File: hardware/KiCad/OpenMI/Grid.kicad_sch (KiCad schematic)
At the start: 42 parts, among them K1 G6DN-1ADC12, Q6 BSS123L, U5 MCP6004-SL, U6 CAP005DG

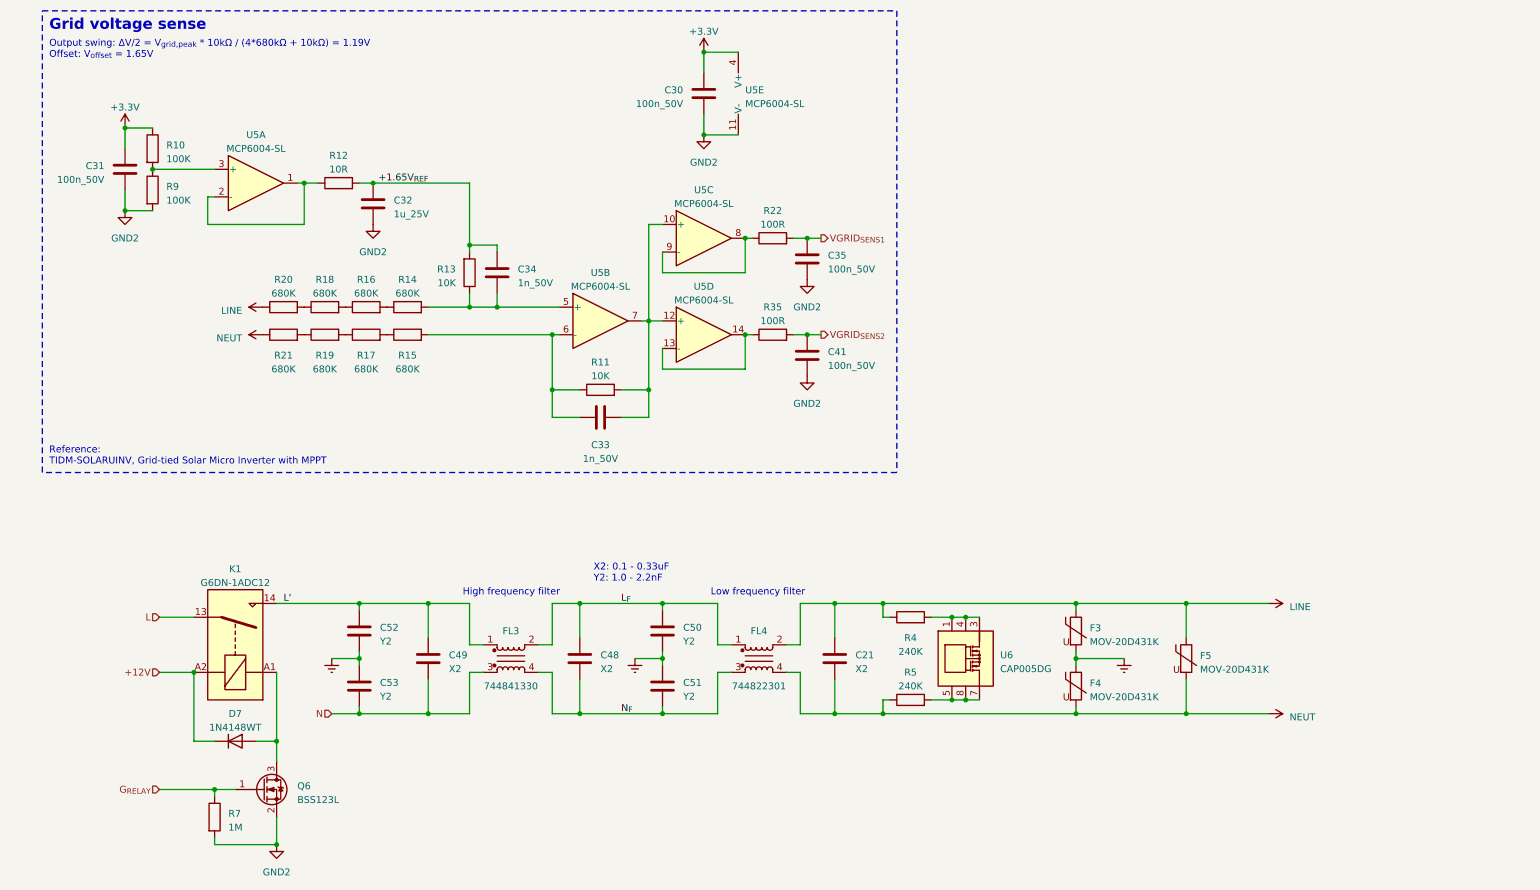
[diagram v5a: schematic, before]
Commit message: refactor(hw): Moves grid voltage sensing to `Sensing`. Refactors labels.
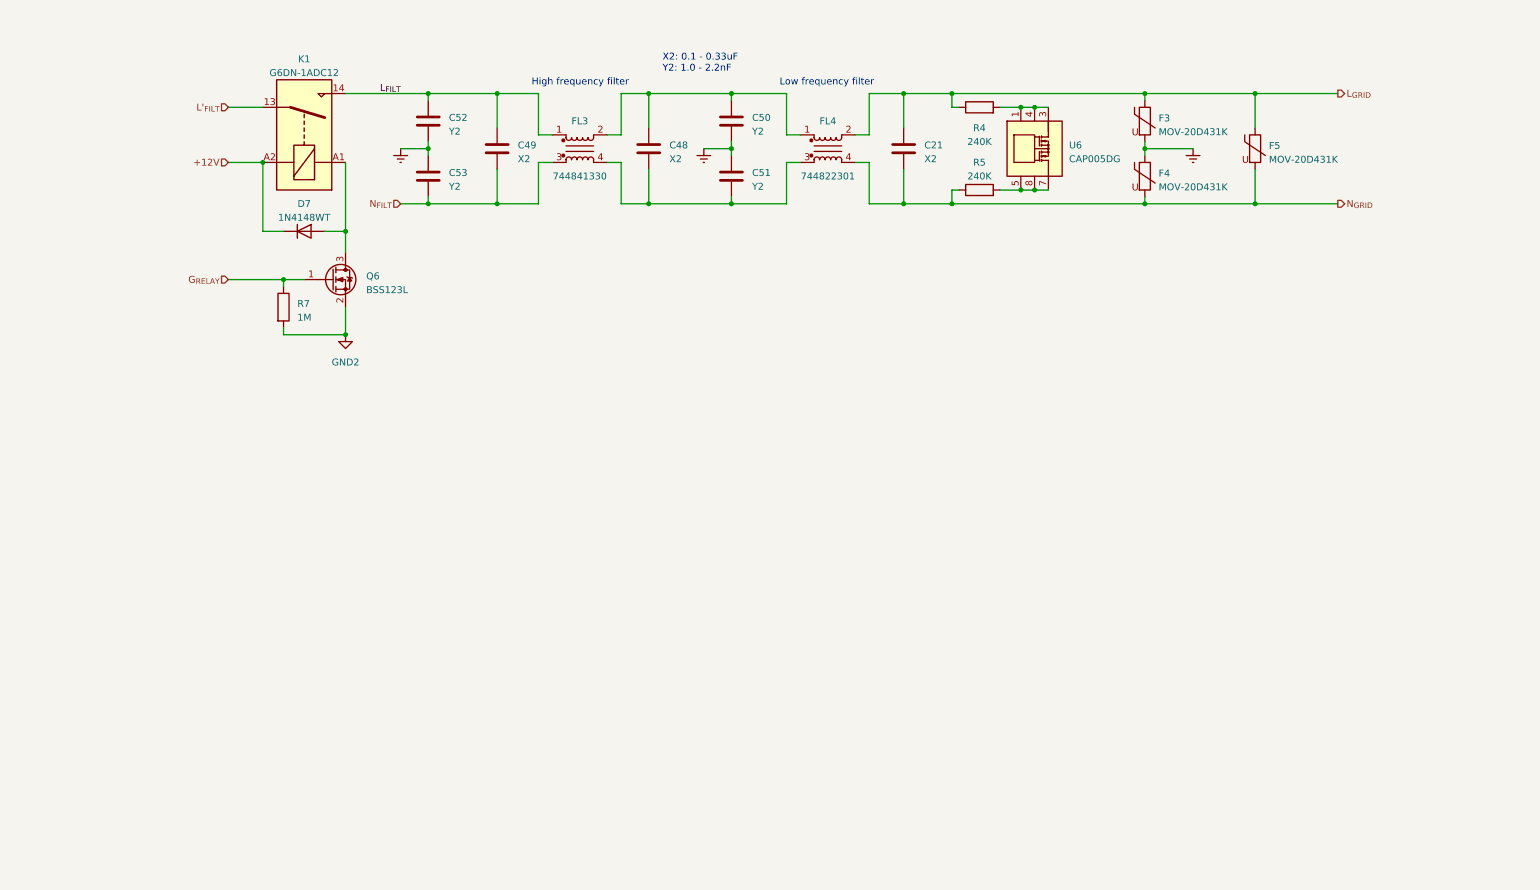
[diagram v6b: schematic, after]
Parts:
- removed C30, C31, C35, C41: 100n_50V, Capacitor_SMD:C_0603_1608Metric, symbol _C_0603:100n_50V
- removed C32: 1u_25V, Capacitor_SMD:C_0805_2012Metric, symbol _C_0805:1u_25V
- removed C33, C34: 1n_50V, Capacitor_SMD:C_0603_1608Metric, symbol _C_0603:1n_50V
- removed R10, R9: 100K, Resistor_SMD:R_0603_1608Metric, symbol _R_0603:100K
- removed R11, R13: 10K, Resistor_SMD:R_0603_1608Metric, symbol _R_0603:10K
- removed R12: 10R, Resistor_SMD:R_0603_1608Metric, symbol _R_0603:10R
- removed R14, R15, R16, R17, R18, R19, R20, R21: 680K, Resistor_SMD:R_1206_3216Metric, symbol _R_1206:680K
- removed R22, R35: 100R, Resistor_SMD:R_0603_1608Metric, symbol _R_0603:100R
- removed U5: MCP6004-SL, Package_SO:SOIC-14_3.9x8.7mm_P1.27mm, symbol _Amplifier_Operational:MCP6004-SL
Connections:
- net L renamed L'_{FILT}
- net L' renamed L_{FILT}
- net LINE renamed L_{GRID}
- net L_{F}: no longer names the net of C48.1, C50.1, FL3.2, FL4.1
- net N renamed N_{FILT}
- net NEUT renamed N_{GRID}
- net N_{F}: no longer names the net of C48.2, C51.2, FL3.4, FL4.3
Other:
- note removed: "Grid voltage sense"
- note removed: "Output swing: ΔV/2 = V_{grid,peak} * 10kΩ / (4*680kΩ + 10kΩ) = 1.19V Offset: V_{offset} = 1.65V"
- note removed: "Reference: TIDM-SOLARUINV, Grid-tied Solar Micro Inverter with MPPT"
- moved on the sheet: C21, C48, C49, C50, C51, C52, C53, D7, F3, F4, F5, FL3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

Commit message: refactor(hw): Adds final safety capacitors to line filter
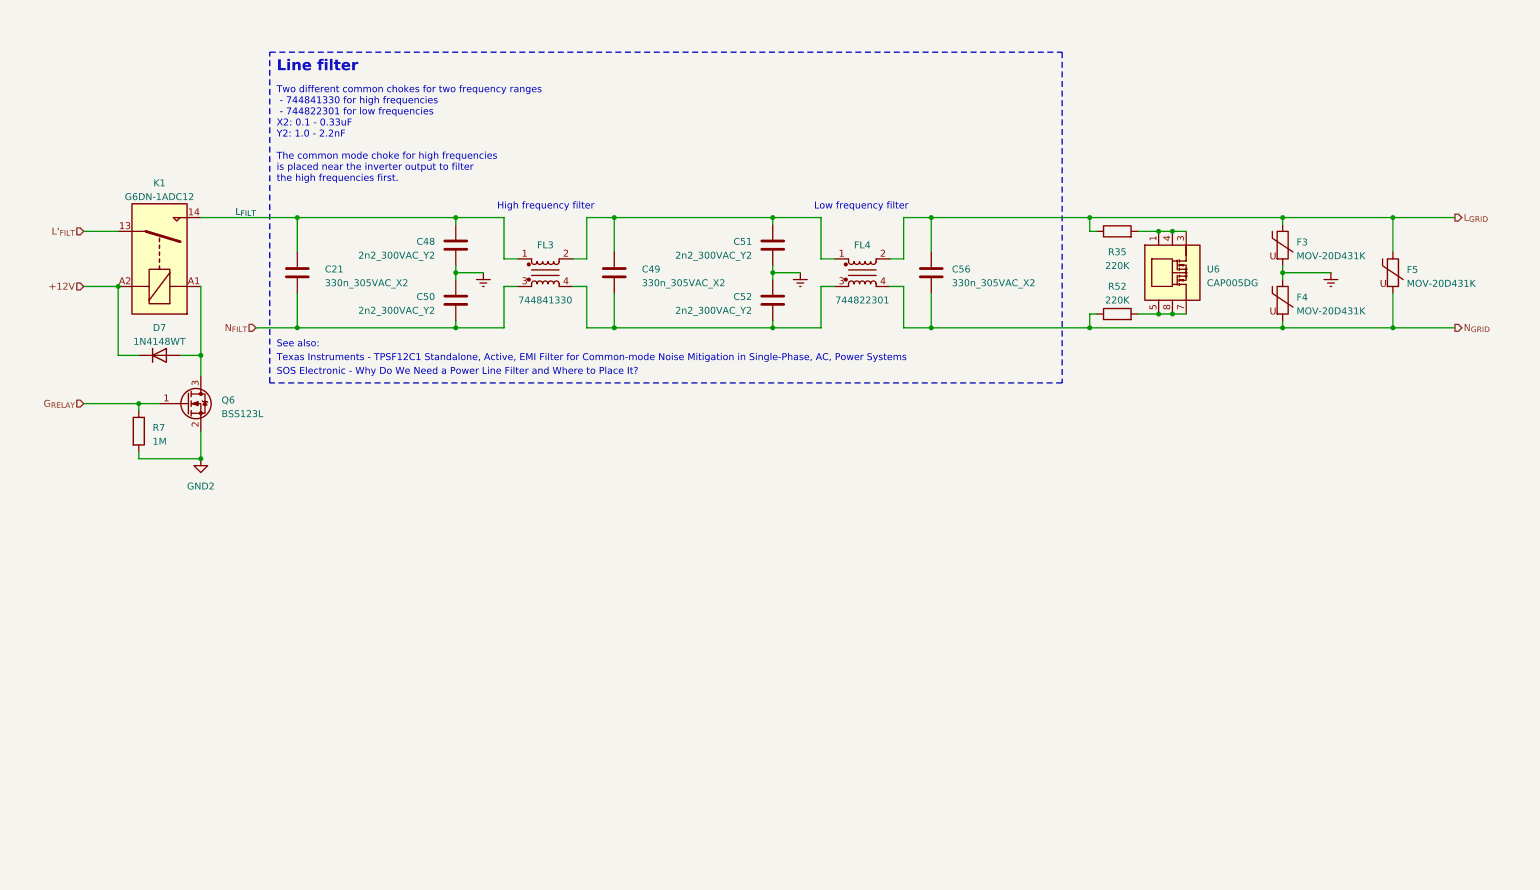
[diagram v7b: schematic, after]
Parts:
- removed C21, C48, C49: X2, symbol Device:C
- removed C50, C51, C52, C53: Y2, symbol Device:C
- removed R4, R5: 240K, Resistor_SMD:R_1206_3216Metric, symbol _R_1206:240K
- added C21, C49, C56: 330n_305VAC_X2, Capacitor_THT:C_Rect_L18.0mm_W8.0mm_P15.00mm_FKS3_FKP3, symbol _C_Safety:330n_305VAC_X2
- added C48, C50, C51, C52: 2n2_300VAC_Y2, Capacitor_THT:C_Rect_L13.0mm_W4.0mm_P10.00mm_FKS3_FKP3_MKS4, symbol _C_Safety:2n2_300VAC_Y2
- added R35, R52: 220K, Resistor_SMD:R_1206_3216Metric, symbol _R_1206:220K
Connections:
- net Earth: now also C48.2, C50.1, C51.2, C52.1
- net L_{FILT}: now also C21.1, C48.1
- net L_{GRID}: now also C56.1, R35.1
- net N_{FILT}: now also C21.2, C50.2
- net N_{GRID}: now also C56.2, R52.1
- net at FL3.2, FL4.1: now also C49.1, C51.1
- net at FL3.4, FL4.3: now also C49.2, C52.2
- net at U6.1, U6.2, U6.3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: now also R35.2
- net at U6.5, U6.6, U6.7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: now also R52.2
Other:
- note added: "Line filter"
- note added: "SOS Electronic - Why Do We Need a Power Line Filter and Where to Place It?"
- note added: "See also:"
- note added: "Texas Instruments - TPSF12C1 Standalone, Active, EMI Filter for Common-mode Noise Mitigation in Single-Phase, AC, Power Systems"
- note added: "Two different common chokes for two frequency ranges - 744841330 for high frequencies - 744822301 for low frequencies X2: 0.1 - 0.33uF Y2: 1.0 - 2.2nF The common mode choke for high frequencies is placed near the inverter output to filter the high frequencies first."
- note removed: "X2: 0.1 - 0.33uF Y2: 1.0 - 2.2nF"
- moved on the sheet: D7, F3, F4, F5, FL3, FL4, K1, Q6, R7, U6

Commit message: feat: Replaces SPST relay with DPDT relay to disconnect "neutral" as well.
docs: Add references to international standards for grid connected devices.
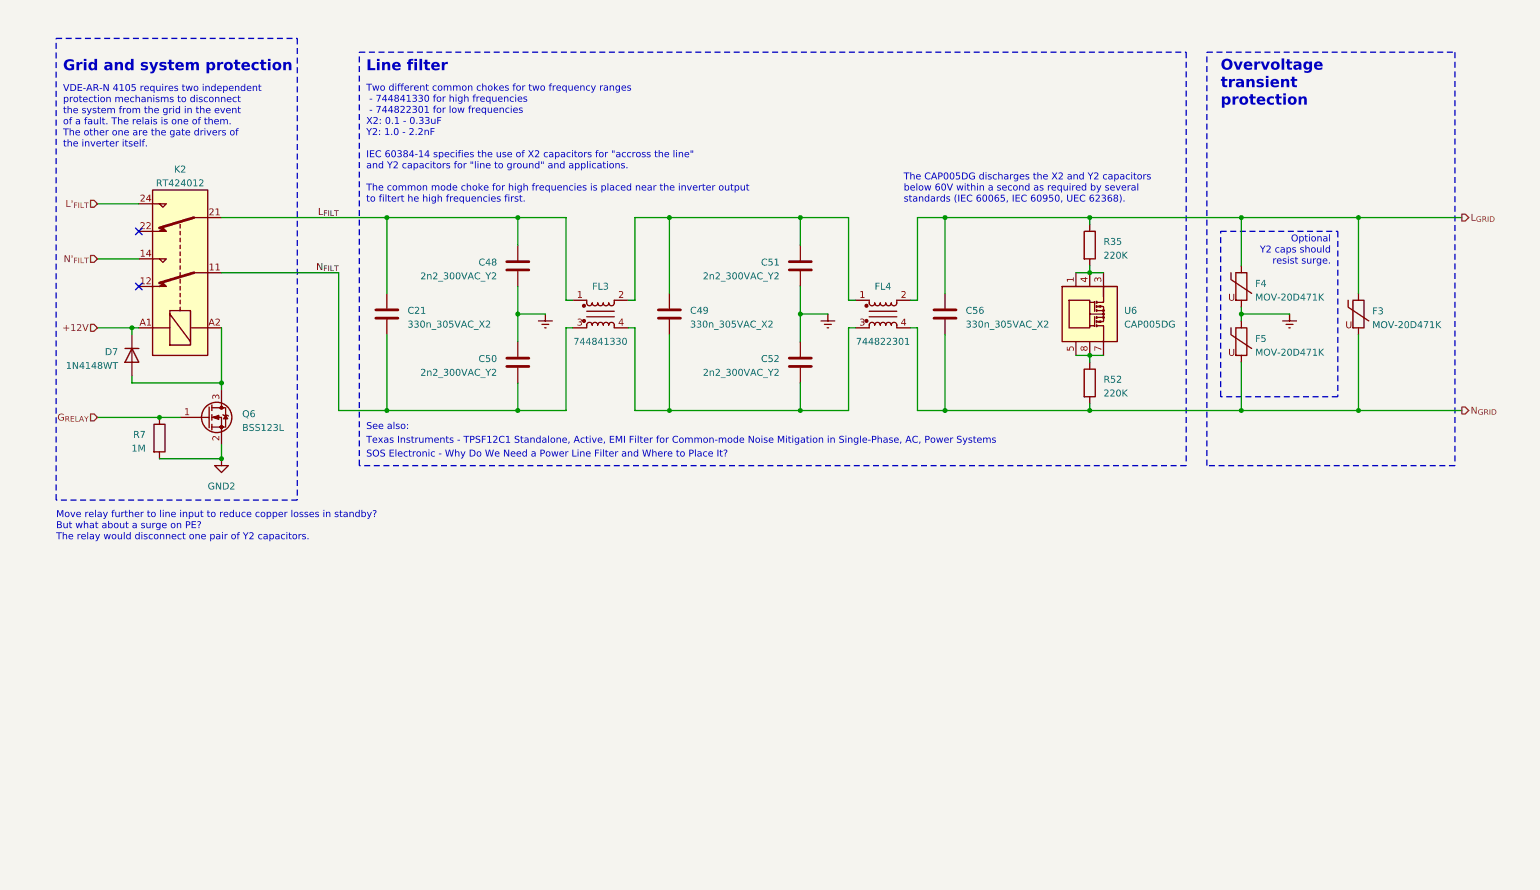
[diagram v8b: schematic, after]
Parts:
- removed F3, F4, F5: MOV-20D431K, Varistor:RV_Disc_D21.5mm_W5.6mm_P10mm, symbol _Varistor:MOV-20D431K
- removed K1: G6DN-1ADC12, OpenCE:Relay_SPST_Omron_G6DN-1A, symbol _Relay:G6DN-1ADC12
- added F3, F4, F5: MOV-20D471K, Varistor:RV_Disc_D21.5mm_W5.8mm_P10mm, symbol _Varistor:MOV-20D471K
- added K2: RT424012, Relay_THT:Relay_DPDT_Schrack-RT2-FormC_RM5mm, symbol _Relay:RT424012
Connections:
- net +12V: now also K2.A1
- net Earth: now also F4.2, F5.1
- net L'_{FILT}: now also K2.24
- net L_{FILT}: now also K2.21
- net L_{GRID}: now also F3.1, F4.1
- net N_{FILT}: now also K2.11
- net N_{GRID}: now also R52.2, F3.2, F5.2; no longer R52.1
- net at D7.2 (A), Q6.3 (D): now also K2.A2
- net at U6.5, U6.6, U6.7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: now also R52.1; no longer R52.2
- new net N'_{FILT}: K2.14
- no-connect marks 0 -> 2
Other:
- note added: "Grid and system protection"
- note added: "Move relay further to line input to reduce copper losses in standby? But what about a surge on PE? The relay would disconnect one pair of Y2 capacitors."
- note added: "Optional Y2 caps should resist surge."
- note added: "Overvoltage transient protection"
- note added: "The CAP005DG discharges the X2 and Y2 capacitors below 60V within a second as required by several standards (IEC 60065, IEC 60950, UEC 62368)."
- note added: "Two different common chokes for two frequency ranges - 744841330 for high frequencies - 744822301 for low frequencies X2: 0.1 - 0.33uF Y2: 1.0 - 2.2nF IEC 60384-14 specifies the use of X2 capacitors for "accross the line" and Y2 capacitors for "line to ground" and applications. The common mode choke for high frequencies is placed near the inverter output to filtert he high frequencies first."
- note added: "VDE-AR-N 4105 requires two independent protection mechanisms to disconnect the system from the grid in the event of a fault. The relais is one of them. The other one are the gate drivers of the inverter itself."
- note removed: "High frequency filter"
- note removed: "Low frequency filter"
- note removed: "Two different common chokes for two frequency ranges - 744841330 for high frequencies - 744822301 for low frequencies X2: 0.1 - 0.33uF Y2: 1.0 - 2.2nF The common mode choke for high frequencies is placed near the inverter output to filter the high frequencies first."
- moved on the sheet: C21, C48, C49, C50, C51, C52, C56, D7, FL3, FL4, Q6, R35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
